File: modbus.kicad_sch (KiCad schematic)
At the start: 6 parts, among them U12 MAX485E

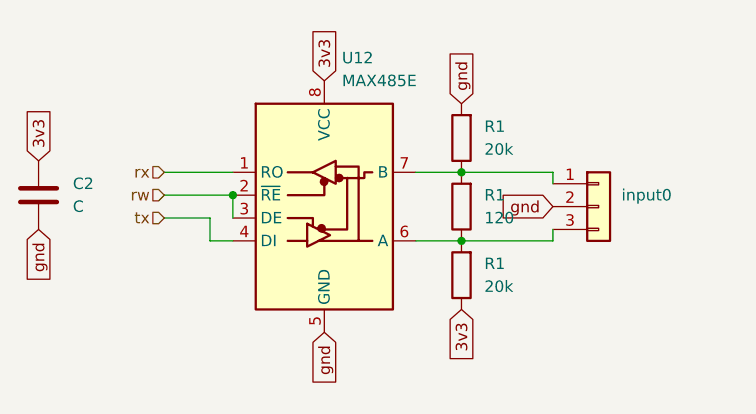
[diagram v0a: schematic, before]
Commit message: fixing labels / add some values
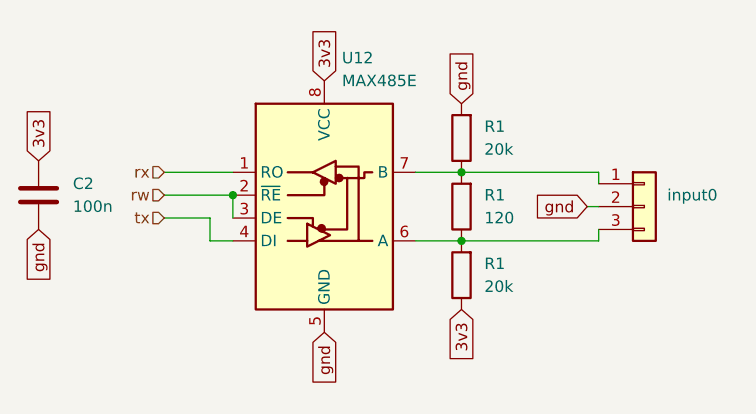
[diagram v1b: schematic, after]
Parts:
- C2: value C -> 100n
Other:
- moved on the sheet: input0
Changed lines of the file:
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@@
+    (stroke (width 0) (type default))
+  )
+  (wire (pts (xy 153.67 81.28) (xy 152.4 81.28))
     (stroke (width 0) (type default))
   )
@@
     (stroke (width 0) (type default))
   )
-  (wire (pts (xy 138.43 85.09) (xy 148.59 85.09))
-    (stroke (width 0) (type default))
-  )
-  (wire (pts (xy 148.59 77.47) (xy 148.59 78.74))
+  (wire (pts (xy 138.43 85.09) (xy 153.67 85.09))
+    (stroke (width 0) (type default))
+  )
+  (wire (pts (xy 153.67 77.47) (xy 153.67 78.74))
     (stroke (width 0) (type default))
   )
@@
     (stroke (width 0) (type default))
   )
-  (wire (pts (xy 148.59 83.82) (xy 148.59 85.09))
-    (stroke (width 0) (type default))
-  )
-  (wire (pts (xy 138.43 77.47) (xy 148.59 77.47))
+  (wire (pts (xy 153.67 83.82) (xy 153.67 85.09))
+    (stroke (width 0) (type default))
+  )
+  (wire (pts (xy 138.43 77.47) (xy 153.67 77.47))
     (stroke (width 0) (type default))
   )
@@
     )
   )
-  (global_label "gnd" (shape input) (at 148.59 81.28 180) (fields_autoplaced)
-    (effects (font (size 1.27 1.27)) (justify right))
-    (property "Intersheetrefs" "${INTERSHEET_REFS}" (at 142.2372 81.28 0)
+  (global_label "gnd" (shape input) (at 152.4 81.28 180) (fields_autoplaced)
+    (effects (font (size 1.27 1.27)) (justify right))
+    (property "Intersheetrefs" "${INTERSHEET_REFS}" (at 146.0472 81.28 0)
       (effects (font (size 1.27 1.27)) (justify right) hide)
     )
@@
       (effects (font (size 1.27 1.27)) (justify left))
     )
-    (property "Value" "C" (at 95.25 81.28 0)
+    (property "Value" "100n" (at 95.25 81.28 0)
       (effects (font (size 1.27 1.27)) (justify left))
     )
@@
     )
   )
-  (symbol (lib_id "Connector_Generic:Conn_01x03") (at 153.67 81.28 0) (unit 1)
-    (in_bom yes) (on_board yes) (dnp no) (fields_autoplaced)
-    (property "Reference" "input0" (at 156.21 80.01 0)
+  (symbol (lib_id "Connector_Generic:Conn_01x03") (at 158.75 81.28 0) (unit 1)
+    (in_bom yes) (on_board yes) (dnp no) (fields_autoplaced)
+    (property "Reference" "input0" (at 161.29 80.01 0)
       (effects (font (size 1.27 1.27)) (justify left))
     )
-    (property "Value" "Conn_01x03" (at 156.21 82.55 0)
-      (effects (font (size 1.27 1.27)) (justify left) hide)
-    )
-    (property "Footprint" "Connector_JST:JST_XH_B3B-XH-A_1x03_P2.50mm_Vertical" (at 153.67 81.28 0)
-      (effects (font (size 1.27 1.27)) hide)
-    )
-    (property "Datasheet" "~" (at 153.67 81.28 0)
-      (effects (font (size 1.27 1.27)) hide)
-    )
+    (property "Value" "Conn_01x03" (at 161.29 82.55 0)
+      (effects (font (size 1.27 1.27)) (justify left) hide)
+    )
+    (property "Footprint" "Connector_JST:JST_XH_B3B-XH-A_1x03_P2.50mm_Vertical" (at 158.75 81.28 0)
+      (effects (font (size 1.27 1.27)) hide)
+    )
+    (property "Datasheet" "~" (at 158.75 81.28 0)
+      (effects (font (size 1.27 1.27)) hide)
+    )
